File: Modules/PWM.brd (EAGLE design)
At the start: 33.1 x 28.8 mm, 32 parts, among them J3 2X6 FEMALE

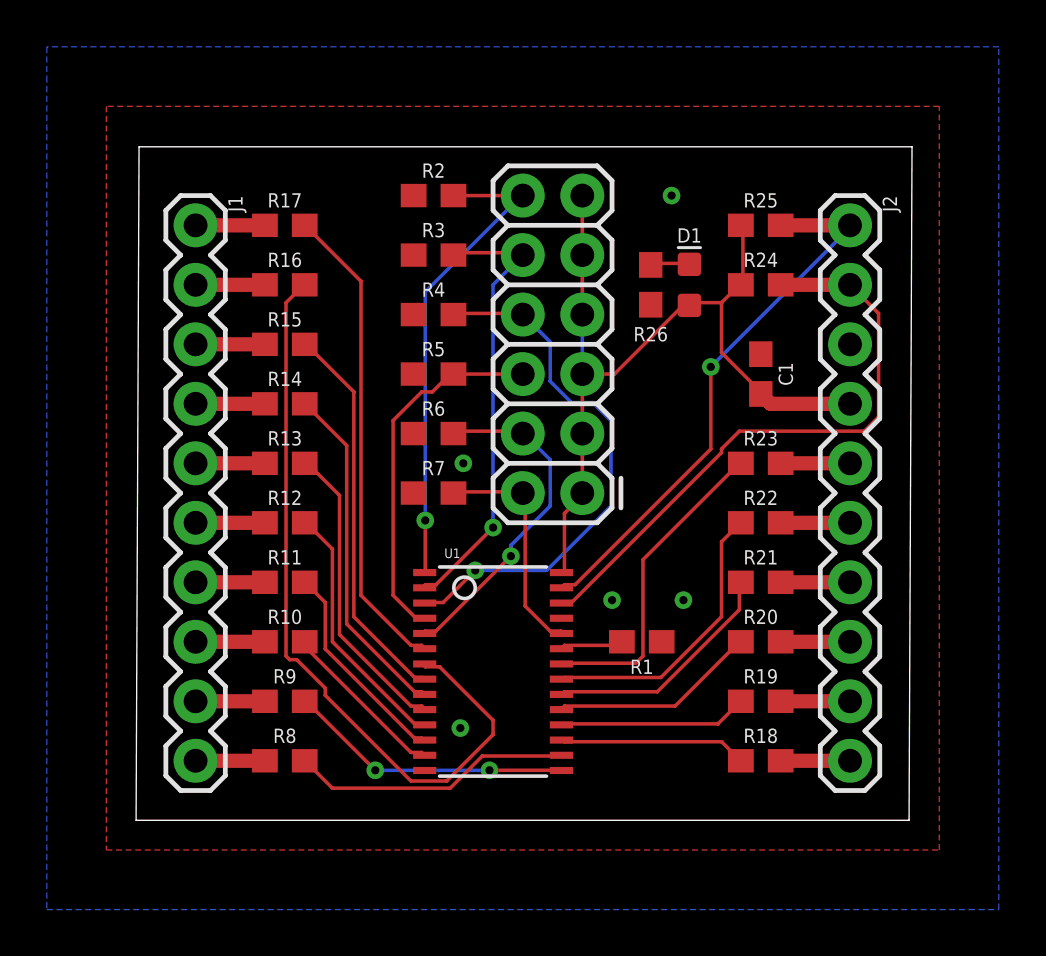
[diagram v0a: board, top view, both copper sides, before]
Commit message: Added modules library
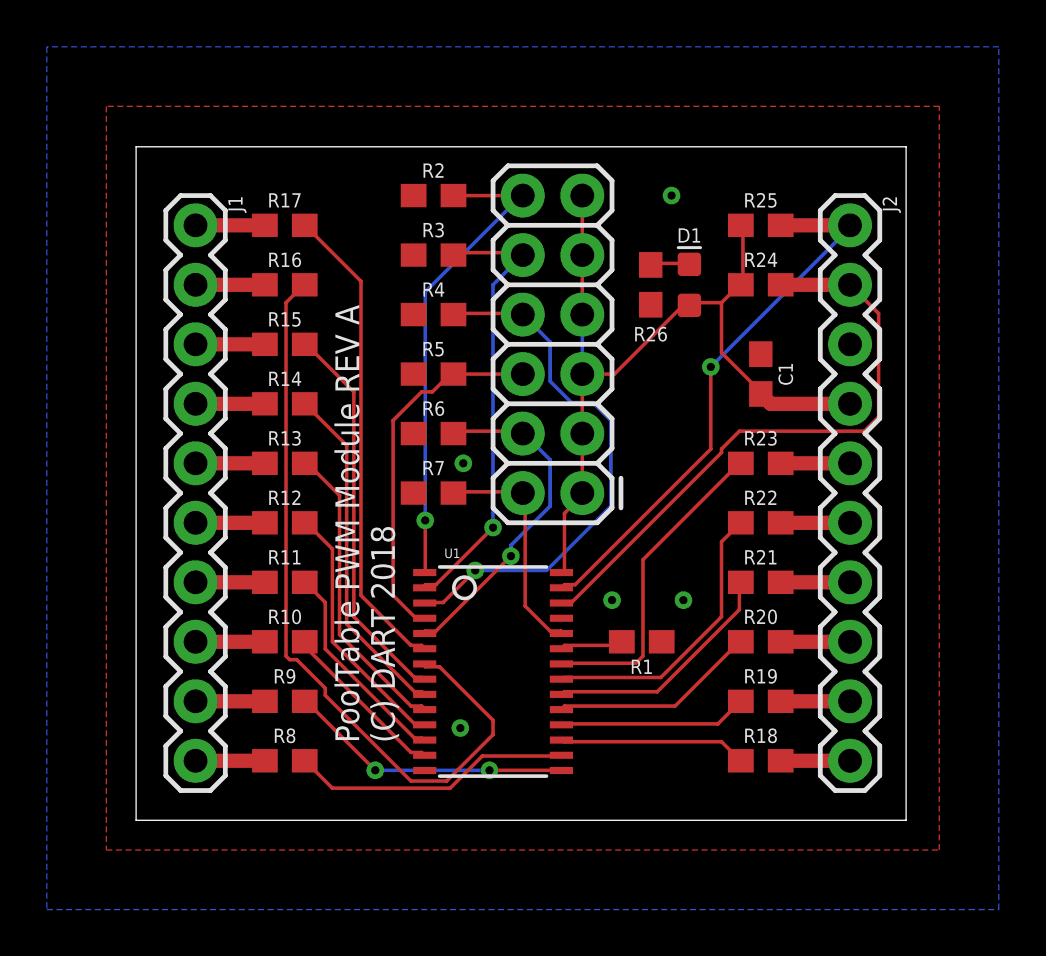
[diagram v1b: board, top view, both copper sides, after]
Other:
- board size 33.1 x 28.8 mm -> 32.9 x 28.8 mm
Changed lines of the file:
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@@
 <grid distance="50" unitdist="mil" unit="mil" style="lines" multiple="1" display="no" altdistance="5" altunitdist="mil" altunit="mil"/>
 <layers>
-<layer number="1" name="Top" color="4" fill="1" visible="no" active="yes"/>
+<layer number="1" name="Top" color="4" fill="1" visible="yes" active="yes"/>
 <layer number="2" name="Route2" color="16" fill="1" visible="no" active="no"/>
 <layer number="3" name="Route3" color="17" fill="1" visible="no" active="no"/>
@@
 <layer number="14" name="Route14" color="22" fill="1" visible="no" active="no"/>
 <layer number="15" name="Route15" color="23" fill="1" visible="no" active="no"/>
-<layer number="16" name="Bottom" color="1" fill="1" visible="no" active="yes"/>
+<layer number="16" name="Bottom" color="1" fill="1" visible="yes" active="yes"/>
 <layer number="17" name="Pads" color="2" fill="1" visible="yes" active="yes"/>
 <layer number="18" name="Vias" color="2" fill="1" visible="yes" active="yes"/>
@@
 <board>
 <plain>
-<wire x1="0" y1="0" x2="33" y2="0" width="0" layer="20"/>
-<wire x1="33" y1="0" x2="33.127" y2="28.753" width="0" layer="20"/>
-<wire x1="33.127" y1="28.753" x2="0.127" y2="28.753" width="0" layer="20"/>
-<wire x1="0.127" y1="28.753" x2="0" y2="0" width="0" layer="20"/>
-<text x="11.049" y="3.302" size="0.6096" layer="48" rot="R90">PoolTable PWM Module
-REV A
+<wire x1="0" y1="0" x2="32.873" y2="0" width="0" layer="20"/>
+<wire x1="32.873" y1="0" x2="32.873" y2="28.753" width="0" layer="20"/>
+<wire x1="32.873" y1="28.753" x2="0" y2="28.753" width="0" layer="20"/>
+<wire x1="0" y1="28.753" x2="0" y2="0" width="0" layer="20"/>
+<text x="11.049" y="3.302" size="1.016" layer="21" rot="R90">PoolTable PWM Module REV A
 (C) DART 2018</text>
 </plain>
@@
 <via x="13.843" y="3.937" extent="1-16" drill="0.35"/>
 <via x="20.32" y="9.398" extent="1-16" drill="0.35"/>
+<wire x1="13.843" y1="3.937" x2="12.3222" y2="2.125" width="0" layer="19" extent="1-1"/>
+<wire x1="11.85" y1="19.05" x2="11.85" y2="16.51" width="0" layer="19" extent="1-1"/>
 </signal>
 <signal name="SDA">

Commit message: Added Connectors and Molex
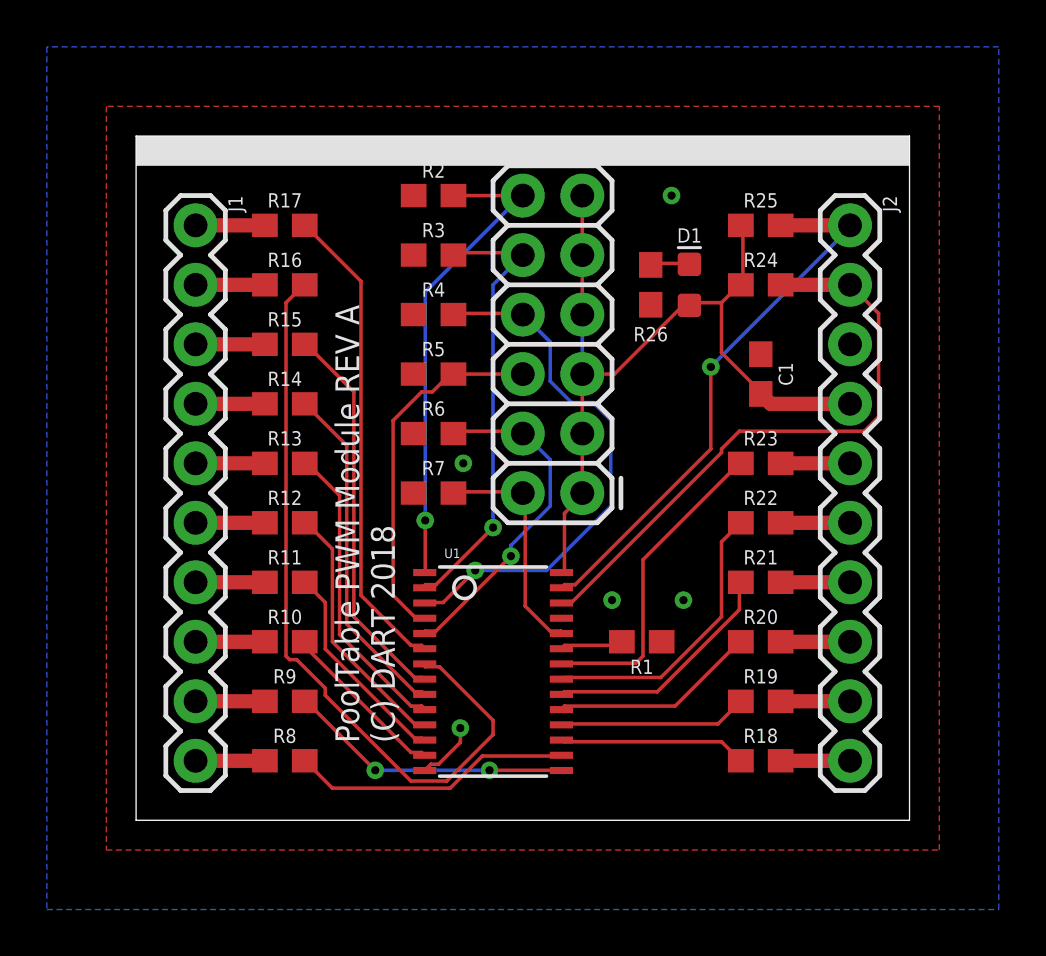
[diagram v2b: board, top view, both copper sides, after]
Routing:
- net GND: track 0.00 -> 2.63 mm
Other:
- board size 32.9 x 28.8 mm -> 33 x 29.2 mm
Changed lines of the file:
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@@
 <?xml version="1.0" encoding="utf-8"?>
 <!DOCTYPE eagle SYSTEM "eagle.dtd">
-<eagle version="9.2.2">
+<eagle version="9.3.0">
 <drawing>
 <settings>
@@
 <setting verticaltext="up"/>
 </settings>
-<grid distance="50" unitdist="mil" unit="mil" style="lines" multiple="1" display="no" altdistance="5" altunitdist="mil" altunit="mil"/>
+<grid distance="50" unitdist="mil" unit="mil" style="lines" multiple="1" display="yes" altdistance="5" altunitdist="mil" altunit="mil"/>
 <layers>
 <layer number="1" name="Top" color="4" fill="1" visible="yes" active="yes"/>
@@
 <board>
 <plain>
-<wire x1="0" y1="0" x2="32.873" y2="0" width="0" layer="20"/>
-<wire x1="32.873" y1="0" x2="32.873" y2="28.753" width="0" layer="20"/>
-<wire x1="32.873" y1="28.753" x2="0" y2="28.753" width="0" layer="20"/>
-<wire x1="0" y1="28.753" x2="0" y2="0" width="0" layer="20"/>
+<wire x1="0" y1="0" x2="33.02" y2="0" width="0" layer="20"/>
+<wire x1="33.02" y1="0" x2="33.02" y2="29.21" width="0" layer="20"/>
+<wire x1="33.02" y1="29.21" x2="0" y2="29.21" width="0" layer="20"/>
+<wire x1="0" y1="29.21" x2="0" y2="0" width="0" layer="20"/>
 <text x="11.049" y="3.302" size="1.016" layer="21" rot="R90">PoolTable PWM Module REV A
 (C) DART 2018</text>
+<rectangle x1="0" y1="27.94" x2="33.02" y2="29.21" layer="21"/>
 </plain>
 <attributes>
@@
 <via x="13.843" y="3.937" extent="1-16" drill="0.35"/>
 <via x="20.32" y="9.398" extent="1-16" drill="0.35"/>
-<wire x1="13.843" y1="3.937" x2="12.3222" y2="2.125" width="0" layer="19" extent="1-1"/>
-<wire x1="11.85" y1="19.05" x2="11.85" y2="16.51" width="0" layer="19" extent="1-1"/>
+<wire x1="12.3222" y1="2.125" x2="12.5912" y2="2.394" width="0.1524" layer="1"/>
+<wire x1="12.5912" y1="2.394" x2="12.9121875" y2="2.394" width="0.1524" layer="1"/>
+<wire x1="12.9121875" y1="2.394" x2="13.843" y2="3.3248125" width="0.1524" layer="1"/>
+<wire x1="13.843" y1="3.3248125" x2="13.843" y2="3.937" width="0.1524" layer="1"/>
 </signal>
 <signal name="SDA">

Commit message: Sending PWM Module to Fab
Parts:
- added U$1: (no value), SparkFun-Aesthetics:OSHW-LOGO-M
- renumbered D1 to PWR
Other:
- board text added: "PoolTable PWM Module Created by DART 2019 Released under the GPLv3"
- board text added: "Rev A"
- board text removed: "PoolTable PWM Module REV A (C) DART 2018"

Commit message: Auto stash before merge of "master" and "origin/master"
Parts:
- R26: value 470 -> 100R
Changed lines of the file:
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@@
 <attribute name="PROD_ID" value="RES-00824" x="41.91" y="-16.51" size="1.778" layer="27" display="off"/>
 </element>
-<element name="R26" library="SparkFun-Resistors" package="0603" value="470" x="21.971" y="22.86" smashed="yes" rot="R270">
+<element name="R26" library="SparkFun-Resistors" package="0603" value="100R" x="21.971" y="22.86" smashed="yes" rot="R270">
 <attribute name="NAME" x="21.971" y="20.447" size="0.6096" layer="25" font="vector" ratio="20" align="bottom-center"/>
 <attribute name="PROD_ID" value="RES-07869" x="-19.939" y="3.81" size="1.778" layer="27" rot="R270" display="off"/>
